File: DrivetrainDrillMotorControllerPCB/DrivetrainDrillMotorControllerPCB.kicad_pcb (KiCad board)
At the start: 2 copper layers, 39 parts, among them J1 DC-005-5A-2.0, J10 Conn_01x02_Socket, J11 Conn_01x02_Socket, J12 Conn_01x02_Socket, J13 Conn_01x02_Socket, J14 Conn_01x02_Socket, J15 Conn_01x02_Socket, J16 Conn_01x02_Socket, J17 Conn_01x08_Socket, J2 Conn_01x02_Socket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

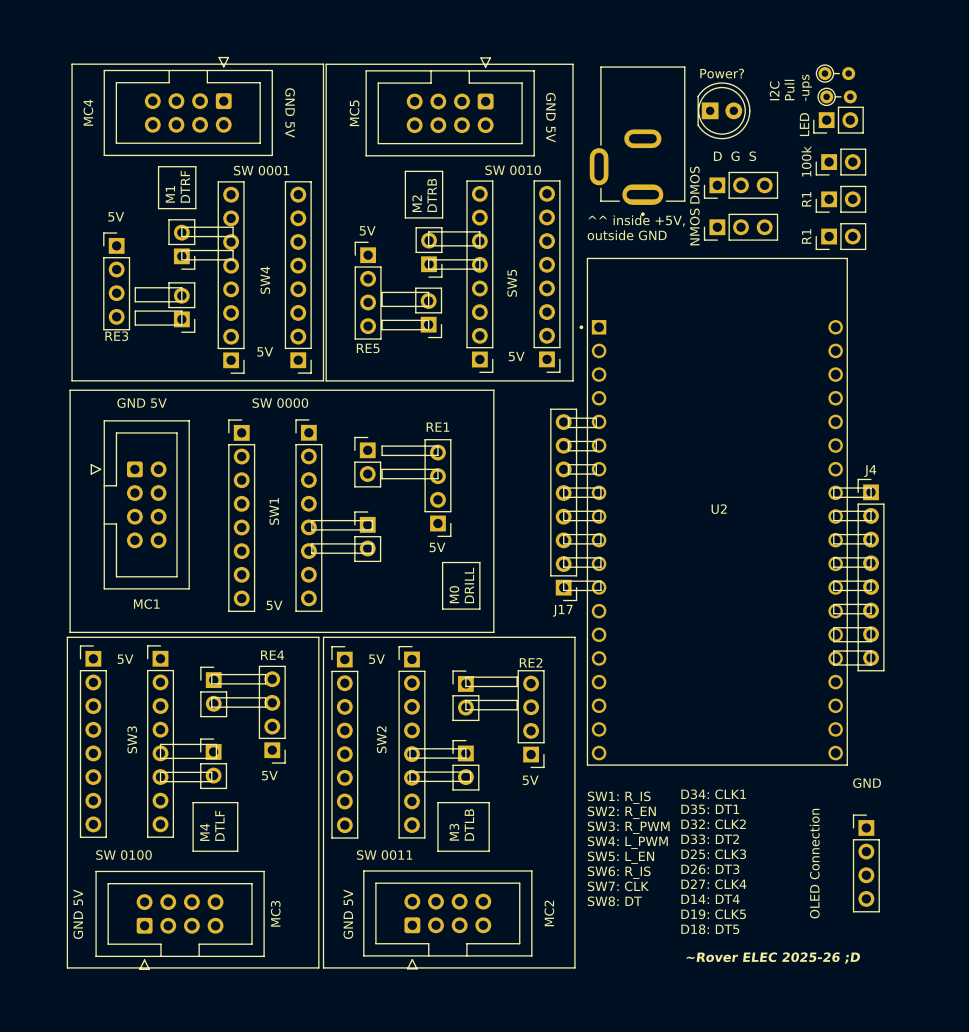
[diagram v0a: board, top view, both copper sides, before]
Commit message: Added copper paths to PCB
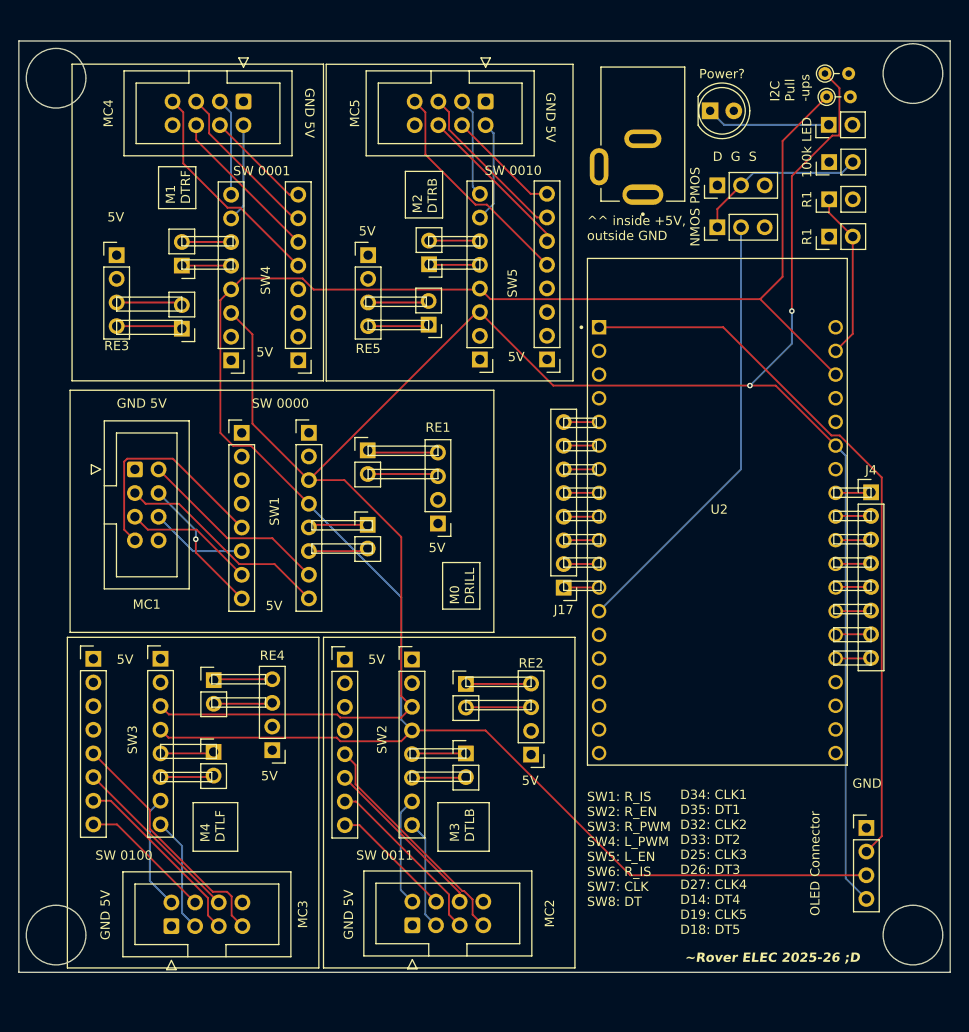
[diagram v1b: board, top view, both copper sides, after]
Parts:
- OLED Connector: renamed from OLED Connection
- moved MC3 2.88 mm to (73.9, 155.0)
- moved MC4 2.12 mm to (81.6, 66.5)
- moved J11 1.00 mm to (75.0, 90.9)
- moved J14 1.00 mm to (75.0, 84.1)
- moved RE3 1.00 mm to (68.0, 83.0)
- moved LED 0.55 mm to (144.5, 69.0)
- renumbered DMOS to PMOS
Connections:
- MC1 pad 8: 5v -> 5V
- MC2 pad 8: 5v -> 5V
- MC3 pad 8: 5v -> 5V
- MC4 pad 8: 5v -> 5V
- MC5 pad 8: 5v -> 5V
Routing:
- net SDA: track 0.00 -> 239.1 mm, vias 0 -> 2
- net SCL: track 0.00 -> 235.1 mm
- net 3.3V: track 0.00 -> 77.9 mm
- net Net-(Q2-G): track 0.00 -> 47.5 mm
- net Net-(MC3-Pin_7): track 0.00 -> 26.1 mm
- net Net-(MC1-Pin_7): track 0.00 -> 24.7 mm
- net Net-(MC2-Pin_7): track 0.00 -> 24.6 mm
- net Net-(MC5-Pin_7): track 0.00 -> 24.1 mm
- net Net-(MC4-Pin_7): track 0.00 -> 24.0 mm
- net Net-(MC1-Pin_3): track 0.00 -> 23.4 mm
- net Net-(MC1-Pin_2): track 0.00 -> 20.8 mm
- net Net-(MC3-Pin_5): track 0.00 -> 20.1 mm
- net Net-(MC2-Pin_5): track 0.00 -> 19.1 mm
- net Net-(MC3-Pin_6): track 0.00 -> 19.0 mm
- net Net-(Q1-G): track 0.00 -> 18.6 mm
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- added copper zone on In2.Cu, net 5V
- added copper zone on In1.Cu, net GND
- added copper zone on In2.Cu, net original5V
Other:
- board outline added: 100 x 100 mm
- copper layers 2 -> 4

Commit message: Modified pcb text
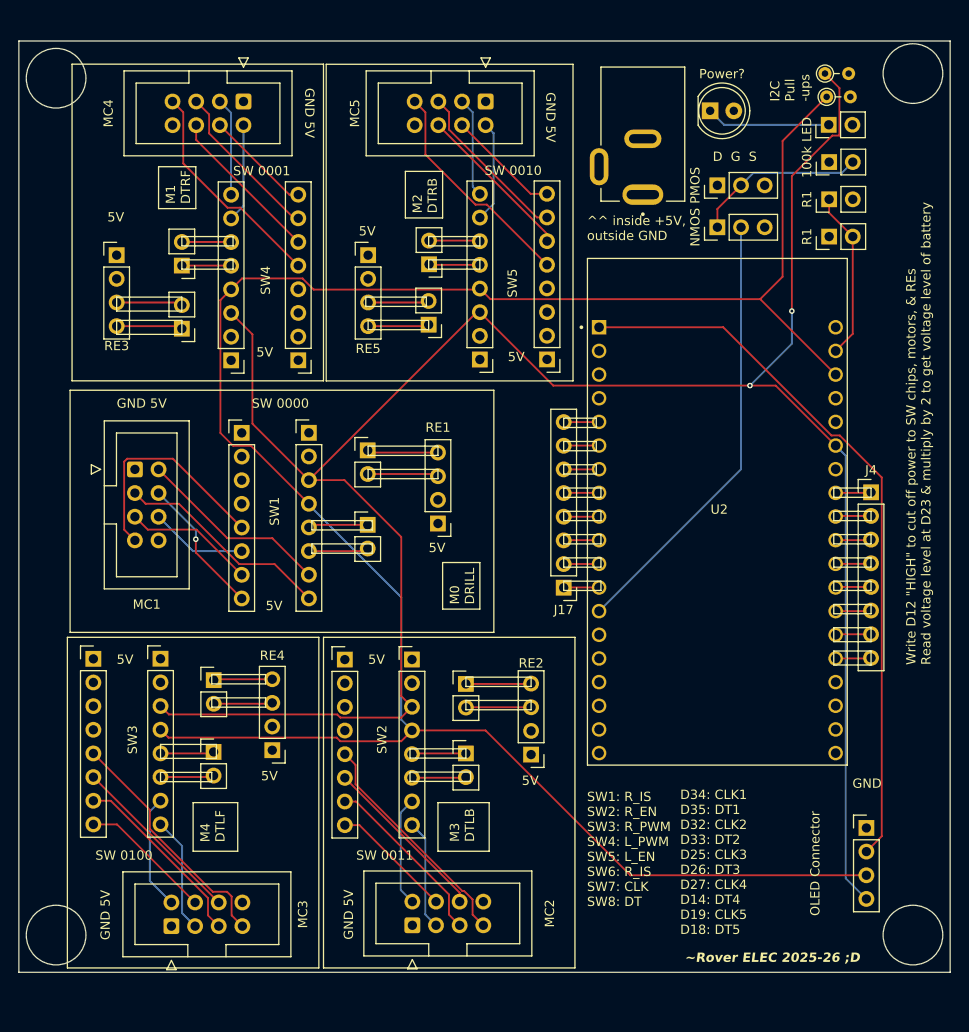
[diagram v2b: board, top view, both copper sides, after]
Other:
- board text added: "Write D12 {dblquote}HIGH{dblquote} to cut off power to SW chips, motors, & REs Read voltage level at D23 & multiply by 2 to get voltage level of battery"
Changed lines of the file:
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@@
 				(font
 					(size 1 1)
-					(thickness 0.1)
+					(thickness 0.15)
 				)
 			)
@@
 				(font
 					(size 1 1)
-					(thickness 0.1)
+					(thickness 0.15)
 				)
 			)
@@
 				(font
 					(size 1 1)
-					(thickness 0.1)
+					(thickness 0.15)
 				)
 			)
@@
 				(font
 					(size 1 1)
-					(thickness 0.1)
+					(thickness 0.15)
 				)
 			)
@@
 				(font
 					(size 1 1)
-					(thickness 0.1)
+					(thickness 0.15)
 				)
 			)
@@
 			(font
 				(size 1 1)
-				(thickness 0.1)
+				(thickness 0.15)
 			)
 			(justify left bottom)
@@
 			(font
 				(size 1 1)
-				(thickness 0.1)
+				(thickness 0.15)
 			)
 			(justify left bottom)
@@
 			(font
 				(size 1 1)
-				(thickness 0.1)
+				(thickness 0.15)
 			)
 			(justify left bottom)
@@
 			(font
 				(size 1 1)
-				(thickness 0.1)
+				(thickness 0.15)
 			)
 			(justify left bottom)
@@
 			(font
 				(size 1 1)
-				(thickness 0.1)
+				(thickness 0.15)
+			)
+			(justify left bottom)
+		)
+	)
+	(gr_text "Write D12 {dblquote}HIGH{dblquote} to cut off power to SW chips, motors, & REs\nRead voltage level at D23 & multiply by 2 to get voltage level of battery"
+		(at 155.5 127 90)
+		(layer "F.SilkS")
+		(effects
+			(font
+				(size 1 1)
+				(thickness 0.15)
 			)
 			(justify left bottom)
@@
 			(font
 				(size 1 1)
-				(thickness 0.1)
+				(thickness 0.15)
 			)
 			(justify left bottom)
@@
 			(font
 				(size 1 1)
-				(thickness 0.1)
+				(thickness 0.15)
 			)
 			(justify left bottom)
@@
 			(font
 				(size 1 1)
-				(thickness 0.1)
+				(thickness 0.15)
 			)
 			(justify left bottom)
@@
 			(font
 				(size 1 1)
-				(thickness 0.1)
+				(thickness 0.15)
 			)
 			(justify left bottom)
@@
 			(font
 				(size 1 1)
-				(thickness 0.1)
+				(thickness 0.15)
 			)
 			(justify left bottom)
@@
 			(font
 				(size 1 1)
-				(thickness 0.1)
+				(thickness 0.15)
 			)
 			(justify left bottom)
@@
 			(font
 				(size 1 1)
-				(thickness 0.1)
+				(thickness 0.15)
 			)
 			(justify left bottom)
@@
 			(font
 				(size 1 1)
-				(thickness 0.1)
+				(thickness 0.15)
 			)
 			(justify left bottom)
@@
 			(font
 				(size 1 1)
-				(thickness 0.1)
+				(thickness 0.15)
 			)
 			(justify left bottom)
@@
 			(font
 				(size 1 1)
-				(thickness 0.1)
+				(thickness 0.15)
 			)
 			(justify left bottom)
@@
 			(font
 				(size 1 1)
-				(thickness 0.1)
+				(thickness 0.15)
 			)
 			(justify left bottom)
@@
 			(font
 				(size 1 1)
-				(thickness 0.1)
+				(thickness 0.15)
 			)
 			(justify left bottom)
@@
 			(font
 				(size 1 1)
-				(thickness 0.1)
+				(thickness 0.15)
 			)
 			(justify left bottom)
@@
 			(font
 				(size 1 1)
-				(thickness 0.1)
+				(thickness 0.15)
 			)
 			(justify left bottom)
@@
 			(font
 				(size 1 1)
-				(thickness 0.1)
+				(thickness 0.15)
 			)
 			(justify left bottom)
@@
 			(font
 				(size 1 1)
-				(thickness 0.1)
+				(thickness 0.15)
 			)
 			(justify left bottom)
@@
 			(font
 				(size 1 1)
-				(thickness 0.1)
+				(thickness 0.15)
 			)
 			(justify left bottom)
@@
 			(font
 				(size 1 1)
-				(thickness 0.1)
+				(thickness 0.15)
 			)
 			(justify left bottom)
@@
 			(font
 				(size 1 1)
-				(thickness 0.1)
+				(thickness 0.15)
 			)
 			(justify left bottom)
@@
 			(font
 				(size 1 1)
-				(thickness 0.1)
+				(thickness 0.15)
 			)
 			(justify left bottom)
@@
 			(font
 				(size 1 1)
-				(thickness 0.1)
+				(thickness 0.15)
 			)
 			(justify left bottom)
@@
 			(font
 				(size 1 1)
-				(thickness 0.1)
+				(thickness 0.15)
 			)
 			(justify left bottom)
@@
 			(font
 				(size 1 1)
-				(thickness 0.1)
+				(thickness 0.15)
 			)
 			(justify left bottom)
@@
 			(font
 				(size 1 1)
-				(thickness 0.125)
+				(thickness 0.15)
 			)
 			(justify left bottom)
@@
 			(font
 				(size 1 1)
-				(thickness 0.1)
+				(thickness 0.15)
 			)
 			(justify left bottom)
@@
 			(font
 				(size 1 1)
-				(thickness 0.1)
+				(thickness 0.15)
 			)
 			(justify left bottom)

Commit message: made screw holes less likely to break
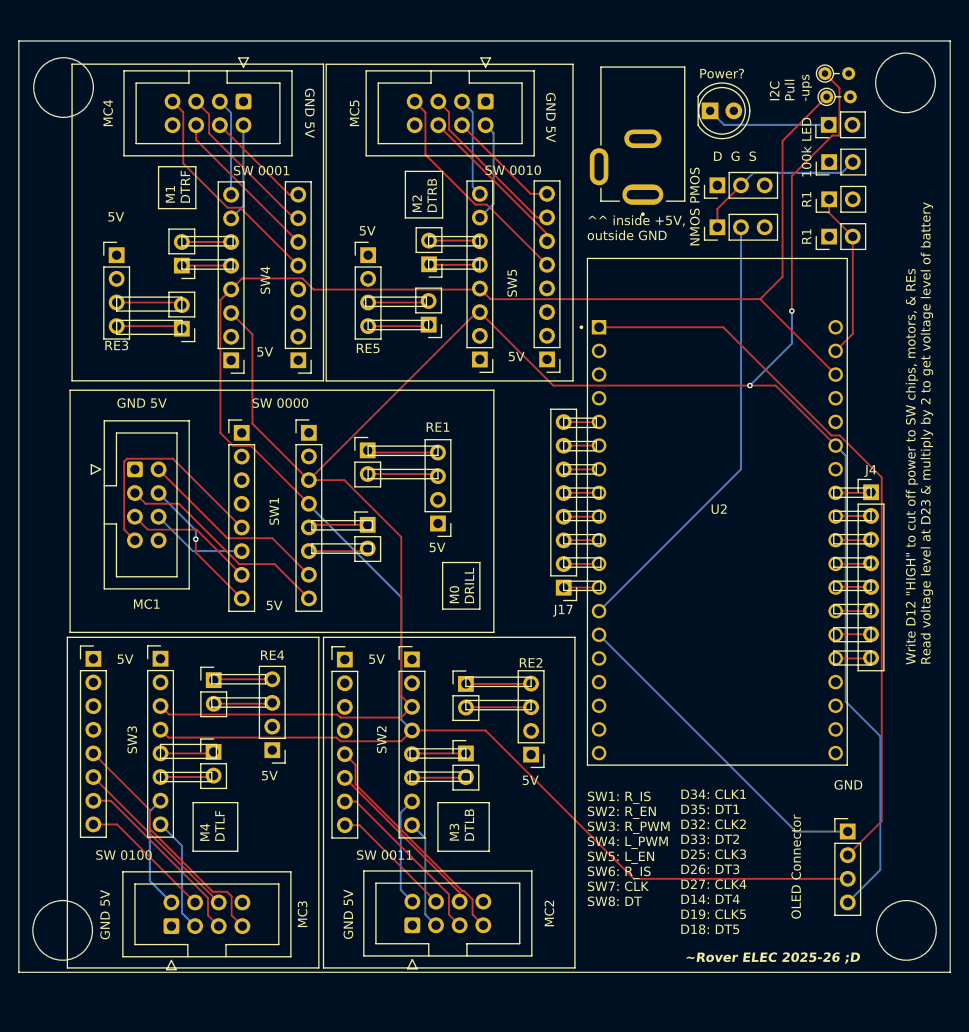
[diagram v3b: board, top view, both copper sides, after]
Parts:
- moved OLED Connector 2.04 mm to (146.5, 144.9)
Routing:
- net GND: track 0.00 -> 35.4 mm
- net SDA: track 239.1 -> 241.6 mm
- net SCL: track 235.1 -> 233.3 mm
- net 3.3V: track 77.9 -> 79.1 mm
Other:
- outline, holes or cut-outs redrawn
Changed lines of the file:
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@@
 	(footprint "Connector_PinHeader_2.54mm:PinHeader_1x04_P2.54mm_Vertical"
 		(layer "F.Cu")
-		(at 148.5 144.5)
+		(at 146.5 144.88)
 		(descr "Through hole straight pin header, 1x04, 2.54mm pitch, single row")
 		(tags "Through hole pin header THT 1x04 2.54mm single row")
@@
 	)
 	(gr_circle
-		(center 153.5 63.5)
-		(end 156 65.5)
+		(center 152.701562 64.5)
+		(end 155.201562 66.5)
 		(stroke
 			(width 0.05)
@@
 	)
 	(gr_circle
-		(center 61.5 64)
-		(end 63.5 66.5)
+		(center 62.298438 65)
+		(end 64.298438 67.5)
 		(stroke
 			(width 0.05)
@@
 	)
 	(gr_circle
-		(center 153.5 156)
-		(end 155.5 158.5)
+		(center 152.798438 155.5)
+		(end 154.798438 158)
 		(stroke
 			(width 0.05)
@@
 	)
 	(gr_circle
-		(center 61.5 156)
-		(end 63.5 158.5)
+		(center 62.201562 155.5)
+		(end 64.201562 158)
 		(stroke
 			(width 0.05)
@@
 	)
 	(gr_text "GND"
-		(at 147 140.31 0)
+		(at 145 140.5 0)
 		(layer "F.SilkS")
 		(effects
@@
 	)
 	(segment
+		(start 146.5 144.88)
+		(end 140.92 144.88)
+		(width 0.2)
+		(layer "B.Cu")
+		(net 7)
+	)
+	(segment
+		(start 140.92 144.88)
+		(end 119.8 123.76)
+		(width 0.2)
+		(layer "B.Cu")
+		(net 7)
+	)
+	(segment
 		(start 69.12484 104.849)
 		(end 74.039 104.849)
@@
 	)
 	(segment
-		(start 99.71 134.03)
-		(end 107.608 134.03)
-		(width 0.2)
-		(layer "F.Cu")
-		(net 70)
-	)
-	(segment
 		(start 81.46 85.5)
 		(end 80.29 86.67)
@@
 	(segment
 		(start 107.608 134.03)
-		(end 123.158 149.58)
+		(end 123.538 149.96)
 		(width 0.2)
 		(layer "F.Cu")
@@
 	)
 	(segment
-		(start 123.158 149.58)
-		(end 148.5 149.58)
-		(width 0.2)
-		(layer "F.Cu")
-		(net 70)
-	)
-	(segment
 		(start 137.101 87.721)
 		(end 139.5 85.322)
@@
 	)
 	(segment
+		(start 99.71 134.03)
+		(end 107.608 134.03)
+		(width 0.2)
+		(layer "F.Cu")
+		(net 70)
+	)
+	(segment
 		(start 89.15876 86.691)
 		(end 87.96776 85.5)
@@
 	)
 	(segment
+		(start 123.538 149.96)
+		(end 146.5 149.96)
+		(width 0.2)
+		(layer "F.Cu")
+		(net 70)
+	)
+	(segment
 		(start 79.139 87.821)
 		(end 79.139 102.091)
@@
 	)
 	(segment
-		(start 140.5 92.5)
-		(end 136 97)
+		(start 146.5 152.5)
+		(end 150 149)
 		(width 0.2)
 		(layer "B.Cu")
@@
 	)
 	(segment
-		(start 148.5 152.12)
-		(end 146.281 149.901)
+		(start 146.281 130.932235)
+		(end 146.281 104.521)
+		(width 0.2)
+		(layer "B.Cu")
+		(net 71)
+	)
+	(segment
+		(start 140.5 92.5)
+		(end 136 97)
 		(width 0.2)
 		(layer "B.Cu")
@@
 	)
 	(segment
-		(start 146.281 149.901)
-		(end 146.281 104.521)
+		(start 150 149)
+		(end 150 134.651235)
+		(width 0.2)
+		(layer "B.Cu")
+		(net 71)
+	)
+	(segment
+		(start 150 134.651235)
+		(end 146.281 130.932235)
 		(width 0.2)
 		(layer "B.Cu")
@@
 	)
 	(segment
-		(start 148.5 147.04)
-		(end 150.151 145.389)
+		(start 150.151 106.862235)
+		(end 150.151 143.769)
 		(width 0.2)
 		(layer "F.Cu")
@@
 	)
 	(segment
+		(start 150.151 143.769)
+		(end 146.5 147.42)
+		(width 0.2)
+		(layer "F.Cu")
+		(net 110)
+	)
+	(segment
 		(start 144.752235 102.359)
 		(end 133.133235 90.74)
@@
 		(width 0.2)
 		(layer "F.Cu")
-		(net 110)
-	)
-	(segment
-		(start 150.151 145.389)
-		(end 150.151 106.862235)
-		(width 0.2)
-		(layer "F.Cu")

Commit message: Filled ground on all layers
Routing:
- net SCL: track 233.3 -> 234.7 mm, vias 0 -> 2
- added copper zone on B.Cu, net GND
- added copper zone on F.Cu, net GND
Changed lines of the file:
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@@
-	)
-	(segment
-		(start 80.29 86.67)
-		(end 79.139 87.821)
-		(width 0.2)
-		(layer "F.Cu")
-		(net 70)
 	)
 	(segment
@@
 	)
 	(segment
+		(start 77.5 89.46)
+		(end 80.29 86.67)
+		(width 0.2)
+		(layer "F.Cu")
+		(net 70)
+	)
+	(segment
 		(start 72.71 133.95)
 		(end 73.56 134.8)
@@
 	)
 	(segment
+		(start 77.5 96.5)
+		(end 77.5 89.46)
+		(width 0.2)
+		(layer "F.Cu")
+		(net 70)
+	)
+	(segment
+		(start 79.139 101)
+		(end 79.139 102.091)
+		(width 0.2)
+		(layer "F.Cu")
+		(net 70)
+	)
+	(segment
 		(start 79.139 102.091)
 		(end 80.517 103.469)
@@
 	)
 	(segment
-		(start 79.139 87.821)
-		(end 79.139 102.091)
-		(width 0.2)
-		(layer "F.Cu")
-		(net 70)
-	)
-	(segment
 		(start 82.419 103.469)
 		(end 88.64 109.69)
@@
 		(net 70)
 	)
+	(via
+		(at 77.5 96.5)
+		(size 0.6)
+		(drill 0.3)
+		(layers "F.Cu" "B.Cu")
+		(net 70)
+	)
+	(via
+		(at 79.139 101)
+		(size 0.6)
+		(drill 0.3)
+		(layers "F.Cu" "B.Cu")
+		(net 70)
+	)
 	(segment
 		(start 98.559 119.72176)
@@
 	)
 	(segment
+		(start 77.5 96.5)
+		(end 77.5 99.5)
+		(width 0.2)
+		(layer "B.Cu")
+		(net 70)
+	)
+	(segment
+		(start 79 101)
+		(end 79.139 101)
+		(width 0.2)
+		(layer "B.Cu")
+		(net 70)
+	)
+	(segment
+		(start 77.5 99.5)
+		(end 79 101)
+		(width 0.2)
+		(layer "B.Cu")
+		(net 70)
+	)
+	(segment
 		(start 88.64 109.69)
 		(end 88.64 109.80276)
@@
 	)
 	(segment
+		(start 80.29 89.21)
+		(end 85 93.92)
+		(width 0.2)
+		(layer "F.Cu")
+		(net 71)
+	)
+	(segment
 		(start 144.055 63.5)
 		(end 145.611 65.056)
@@
 	)
 	(segment
-		(start 82.581 91.501)
-		(end 82.581 101.091)
-		(width 0.2)
-		(layer "F.Cu")
-		(net 71)
-	)
-	(segment
-		(start 80.29 89.21)
-		(end 82.581 91.501)
+		(start 85 103.51)
+		(end 88.64 107.15)
 		(width 0.2)
 		(layer "F.Cu")
@@
 	)
 	(segment
-		(start 82.581 101.091)
-		(end 88.64 107.15)
-		(width 0.2)
-		(layer "F.Cu")
-		(net 71)
-	)
-	(segment
 		(start 92.457 107.15)
 		(end 98.559 113.252)
@@
 		(start 92.02324 132.651)
 		(end 98.549 132.651)
+		(width 0.2)
+		(layer "F.Cu")
+		(net 71)
+	)
+	(segment
+		(start 85 93.92)
+		(end 85 103.51)
 		(width 0.2)
 		(layer "F.Cu")
@@
 	)
 	(zone
+		(net 7)
+		(net_name "GND")
+		(layer "F.Cu")
+		(hatch edge 0.5)
+		(priority 4)
+		(connect_pads
+			(clearance 0.5)
+		)
+		(min_thickness 0.25)
+		(filled_areas_thickness no)
+		(fill yes
+			(thermal_gap 0.5)
+			(thermal_bridge_width 0.5)
+		)
+		(polygon
+			(pts
+				(xy 57.5 60) (xy 157.5 60) (xy 157.5 160) (xy 57.5 160)
+			)
+		)
+	)
+	(zone
+		(net 7)
+		(net_name "GND")
+		(layer "B.Cu")
+		(hatch edge 0.5)
+		(priority 3)
+		(connect_pads
+			(clearance 0.5)
+		)
+		(min_thickness 0.25)
+		(filled_areas_thickness no)
+		(fill yes
+			(thermal_gap 0.5)
+			(thermal_bridge_width 0.5)
+		)
+		(polygon
+			(pts
+				(xy 57.5 60) (xy 157.5 60) (xy 157.5 160) (xy 57.5 159.5)
+			)
+		)
+	)
+	(zone
